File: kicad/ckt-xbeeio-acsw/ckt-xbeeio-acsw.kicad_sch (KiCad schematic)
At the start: 43 parts, among them J1 Screw_Terminal_01x02, J2 Screw_Terminal_01x02, J3 Screw_Terminal_01x02, J4 Screw_Terminal_01x02, J5 Conn_AVR_TagConnect_TC2030, K1 ADJH23xxx, K2 ADJH23xxx, K3 ADJH23xxx, U1 RAC03E-12SK_277, U2 AP63203WU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

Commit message: Layout completed
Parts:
- added H1, H2, H3, H4: MountingHole, MountingHole:MountingHole_3.2mm_M3_Pad, symbol Mechanical:MountingHole_Pad
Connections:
- net Line: now reaches J4.2 (Pin_2), U1.1 (VAC_IN(L))
- net Neutral: now reaches J4.1 (Pin_1), U1.2 (VAC_IN(N))
- net at U3.23 (PC0): now also U4.6 (I6); no longer U4.1 (I1)
- net at U3.24 (PC1): now also U4.5 (I5); no longer U4.2 (I2)
- net at U3.25 (PC2): now also U4.4 (I4); no longer U4.3 (I3)
- net at U3.26 (PC3): now also U4.3 (I3); no longer U4.4 (I4)
- net at U3.27 (PC4): now also U4.2 (I2); no longer U4.5 (I5)
- net at U3.28 (PC5): now also U4.1 (I1); no longer U4.6 (I6)
- net at K1.1: now also U4.12 (O5); no longer U4.16 (O1)
- net at K1.2: now also U4.11 (O6); no longer U4.15 (O2)
- net at K3.1: now also U4.15 (O2); no longer U4.12 (O5)
- net at K3.2: now also U4.16 (O1); no longer U4.11 (O6)
- net at U4.13 (O4): now also K2.1; no longer K2.2
- net at U4.14 (O3): now also K2.2; no longer K2.1

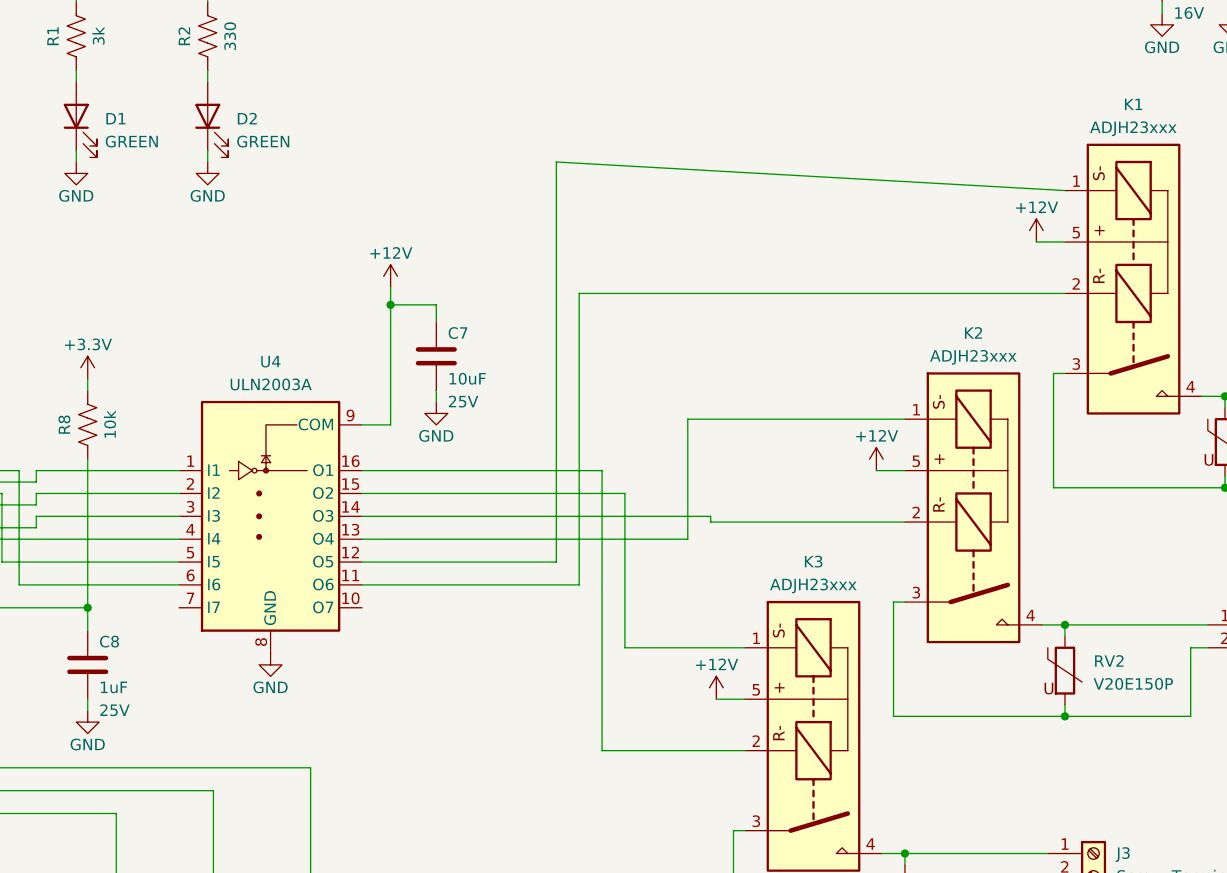
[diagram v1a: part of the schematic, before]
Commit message: Improved metalization, added text
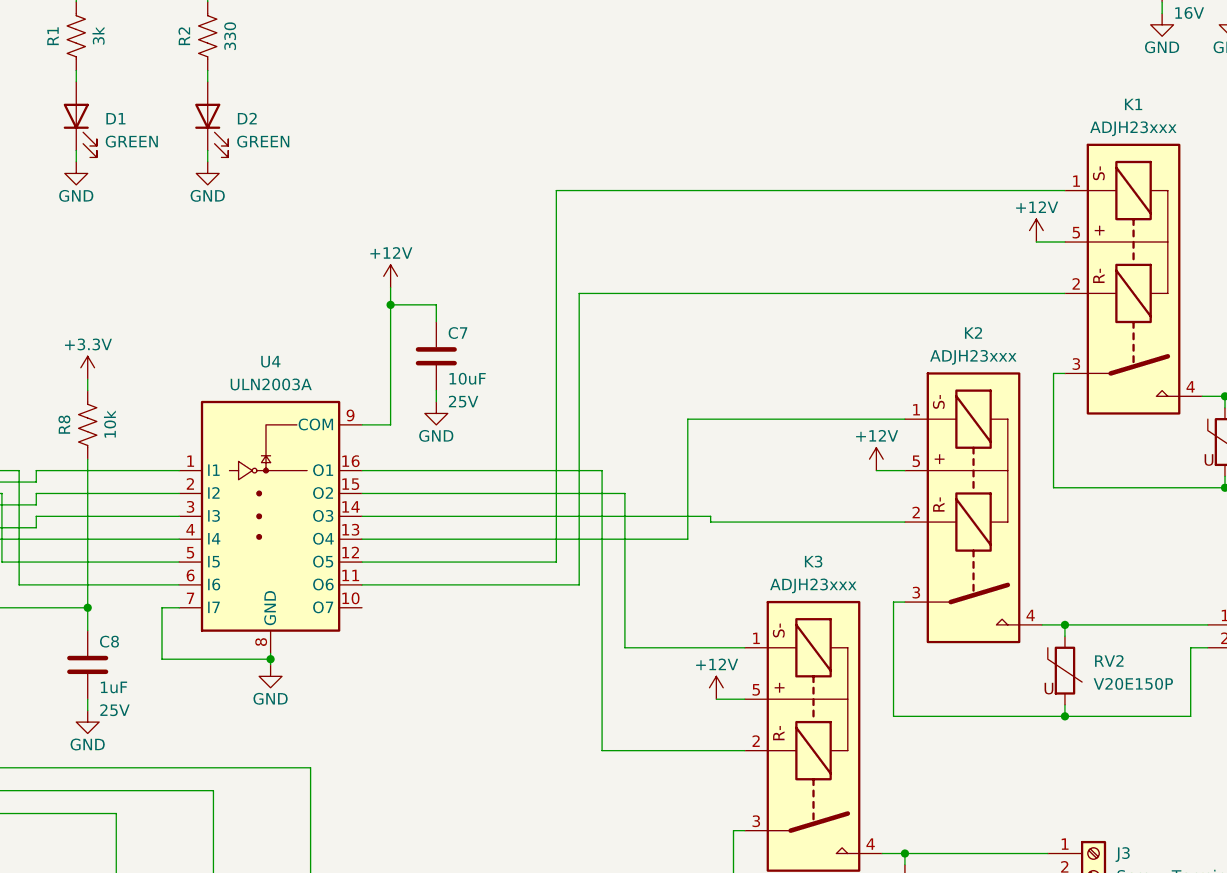
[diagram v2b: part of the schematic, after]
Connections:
- net GND: now also U4.7 (I7)
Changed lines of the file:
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@@
   (junction (at 73.025 122.555) (diameter 0) (color 0 0 0 0)
   )
+  (junction (at 111.76 128.27) (diameter 0) (color 0 0 0 0)
+  )
   (junction (at 212.725 24.13) (diameter 0) (color 0 0 0 0)
   )
@@
     (stroke (width 0) (type default) (color 0 0 0 0))
   )
+  (wire (pts (xy 99.695 128.27) (xy 111.76 128.27))
+    (stroke (width 0) (type default) (color 0 0 0 0))
+  )
   (wire (pts (xy 80.01 112.395) (xy 80.01 114.935))
     (stroke (width 0) (type default) (color 0 0 0 0))
@@
     (stroke (width 0) (type default) (color 0 0 0 0))
   )
+  (wire (pts (xy 101.6 122.555) (xy 99.695 122.555))
+    (stroke (width 0) (type default) (color 0 0 0 0))
+  )
   (wire (pts (xy 266.7 45.085) (xy 273.685 45.085))
     (stroke (width 0) (type default) (color 0 0 0 0))
@@
     (stroke (width 0) (type default) (color 0 0 0 0))
   )
+  (wire (pts (xy 200.025 76.2) (xy 143.51 76.2))
+    (stroke (width 0) (type default) (color 0 0 0 0))
+  )
   (wire (pts (xy 91.44 97.155) (xy 91.44 98.425))
     (stroke (width 0) (type default) (color 0 0 0 0))
@@
     (stroke (width 0) (type default) (color 0 0 0 0))
   )
+  (wire (pts (xy 143.51 76.2) (xy 143.51 117.475))
+    (stroke (width 0) (type default) (color 0 0 0 0))
+  )
   (wire (pts (xy 224.155 45.085) (xy 236.22 45.085))
     (stroke (width 0) (type default) (color 0 0 0 0))
@@
     (stroke (width 0) (type default) (color 0 0 0 0))
   )
+  (wire (pts (xy 111.76 128.905) (xy 111.76 128.27))
+    (stroke (width 0) (type default) (color 0 0 0 0))
+  )
   (wire (pts (xy 217.805 99.06) (xy 217.805 100.33))
     (stroke (width 0) (type default) (color 0 0 0 0))
@@
     (stroke (width 0) (type default) (color 0 0 0 0))
   )
+  (wire (pts (xy 111.76 128.27) (xy 111.76 127.635))
+    (stroke (width 0) (type default) (color 0 0 0 0))
+  )
   (wire (pts (xy 55.88 74.93) (xy 55.88 76.835))
     (stroke (width 0) (type default) (color 0 0 0 0))
@@
     (stroke (width 0) (type default) (color 0 0 0 0))
   )
+  (wire (pts (xy 99.695 122.555) (xy 99.695 128.27))
+    (stroke (width 0) (type default) (color 0 0 0 0))
+  )
   (wire (pts (xy 226.695 84.455) (xy 226.695 85.725))
     (stroke (width 0) (type default) (color 0 0 0 0))
   )
-  (wire (pts (xy 143.51 73.025) (xy 200.025 76.2))
-    (stroke (width 0) (type default) (color 0 0 0 0))
-  )
   (wire (pts (xy 200.025 87.63) (xy 146.05 87.63))
     (stroke (width 0) (type default) (color 0 0 0 0))
@@
   )
   (wire (pts (xy 85.725 109.855) (xy 101.6 109.855))
-    (stroke (width 0) (type default) (color 0 0 0 0))
-  )
-  (wire (pts (xy 143.51 73.025) (xy 143.51 117.475))
     (stroke (width 0) (type default) (color 0 0 0 0))
   )
@@
     (pin "2")
   )
-  (symbol (lib_id "power:GND") (at 111.76 127.635 0) (unit 1)
-    (in_bom yes) (on_board yes)
-    (property "Reference" "#PWR0120" (id 0) (at 111.76 133.985 0)
-      (effects (font (size 1.27 1.27)) hide)
-    )
-    (property "Value" "GND" (id 1) (at 111.76 131.445 0))
-    (property "Footprint" "" (id 2) (at 111.76 127.635 0)
-      (effects (font (size 1.27 1.27)) hide)
-    )
-    (property "Datasheet" "" (id 3) (at 111.76 127.635 0)
-      (effects (font (size 1.27 1.27)) hide)
-    )
+  (symbol (lib_id "power:GND") (at 111.76 128.905 0) (unit 1)
+    (in_bom yes) (on_board yes)
+    (property "Reference" "#PWR0120" (id 0) (at 111.76 135.255 0)
+      (effects (font (size 1.27 1.27)) hide)
+    )
+    (property "Value" "GND" (id 1) (at 111.76 132.715 0))
+    (property "Footprint" "" (id 2) (at 111.76 128.905 0)
+      (effects (font (size 1.27 1.27)) hide)
+    )
+    (property "Datasheet" "" (id 3) (at 111.76 128.905 0)
+      (effects (font (size 1.27 1.27)) hide)
+    )

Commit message: Small improvements
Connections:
- net ~{RESET}: now reaches C8.1, J5.5 (~{RESET}), R8.1, U3.29 (~{RESET}/PC6)
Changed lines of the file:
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@@
     (effects (font (size 1.27 1.27)) (justify right bottom))
+  )
+  (label "~{RESET}" (at 76.2 122.555 0)
+    (effects (font (size 1.27 1.27)) (justify left bottom))
   )
   (label "IN2" (at 273.685 47.625 180)
